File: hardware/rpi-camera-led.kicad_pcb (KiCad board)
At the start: 2 copper layers, 25 x 23.9 mm, 20 parts, among them J1 FFC 15P 1.0mm (to Raspberry P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, J2 FFC 15P 1.0mm (to camera), J3 Qwiic (JST SH 1.0mm), J4 SWD program header 2.54mm, Q1 AO3400A, Q2 Phototransistor, U1 CH32V003A4M6

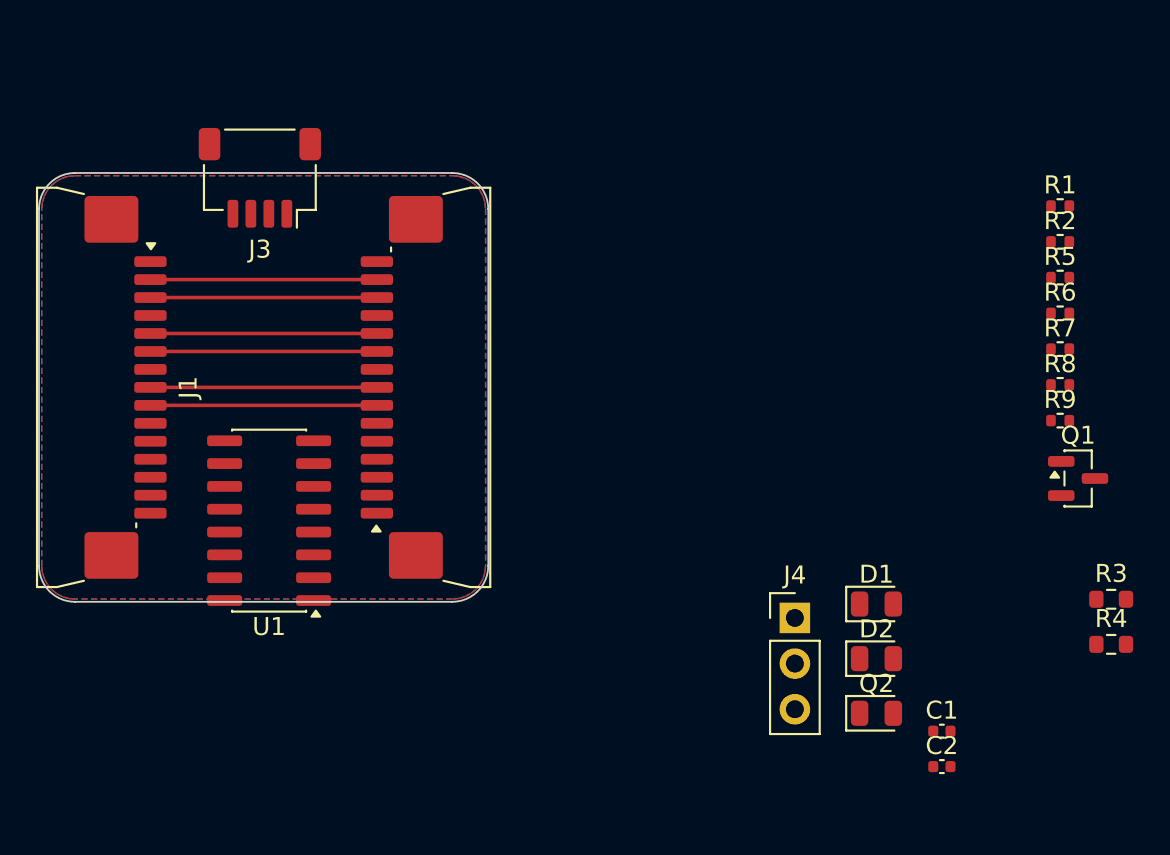
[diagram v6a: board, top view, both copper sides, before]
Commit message: Tim's KiCad session: U1 pins rearranged, bus routing extended
Committing work in progress so it is not lost.  U1's assignment moves
toward the arrangement Tim asked about -- camera GPIOs on pins 7/8, Pi
sense on 9/10, I2C also brought out to 5/6 and 11/12 -- J2 goes back to
the reversed pin mapping, and the board grows to 37 track segments with
unconnected down from 49 to 35.

It does not pass its checks yet.  Recorded here rather than fixed,
because each of these is a design decision:

  * ERC error, U1.13 (PA2) is connected to nothing, with a 0.038mm wire
    fragment left behind at the same point -- the remains of dragging
    CAM_IO1 off that pin.
  * SWIO and CAM_IO1 are the same net.  U1.7 is PD1, the single-wire
    debug pin, and J4.2 sits on it, so KiCad merges the two and keeps
    CAM_IO1.  Programming the part would drive the camera's GPIO1 and
    the camera would fight the debugger.
  * SCL is wired to U1.11 and SDA to U1.12, which are PD7 and PA1.
    Neither can be I2C on this package -- the peripheral only reaches
    PC1/PC2 (pins 1/2), since both AFIO remaps need PD0 or PC5 and the
    SOP-16 bonds out neither.  PD7 is worse than useless here: it is
    NRST until the RST_MODE option byte says otherwise, so a factory
    part would sit in reset for every low half-cycle of SCL.  SDA on
    U1.5 and SCL on U1.6 (PC6/PC7) are inert rather than harmful.
  * Four no-connect flags now dangle where pins used to be.

The board matches the schematic (parity 0), so the same joins exist in
copper: 116 DRC violations.

Co-Authored-By: Claude Opus 5 (1M context) <noreply@anthropic.com>
Claude-Session: https://claude.ai/code/session_01E6VQHygrbAGSqdngQQsBdx
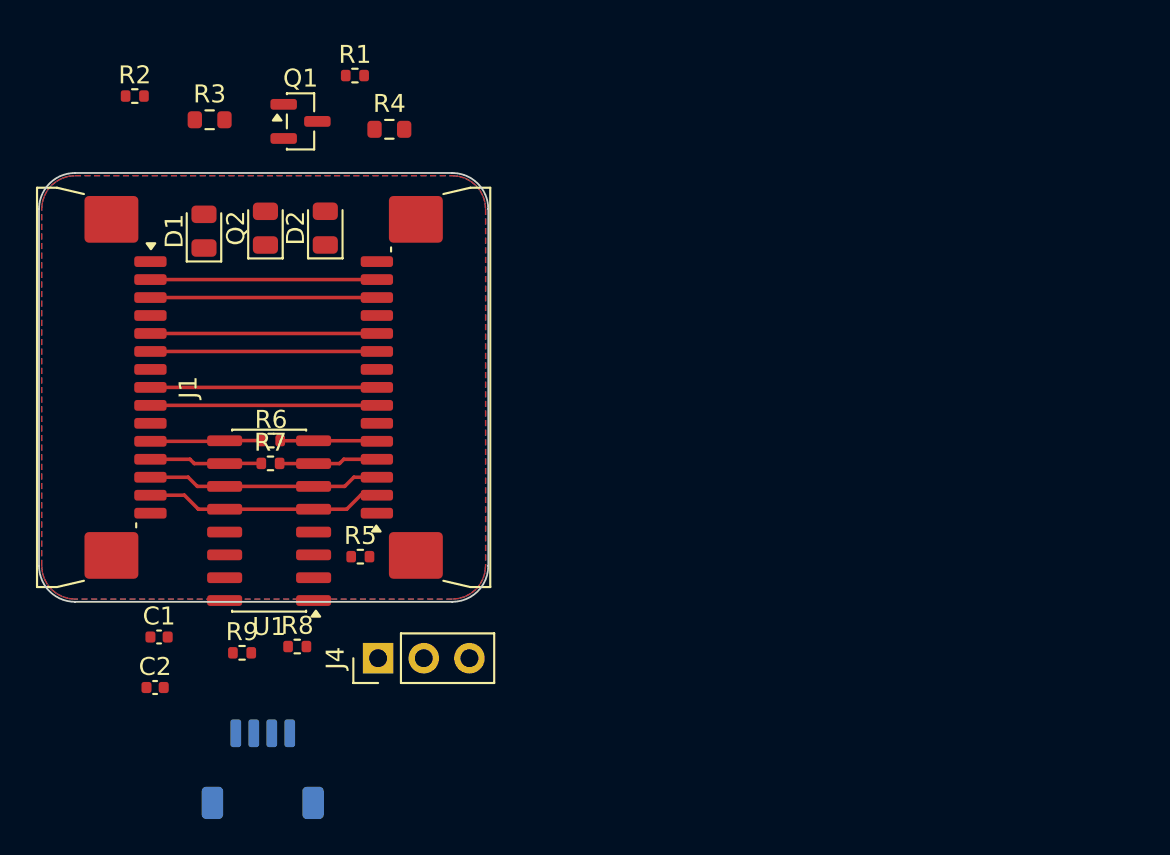
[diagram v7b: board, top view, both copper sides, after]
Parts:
- J3: moved to B.Cu
- moved R3 56.8 mm to (29.5, 17.0)
- moved R2 52.1 mm to (25.3, 15.7)
- moved R4 49.3 mm to (39.5, 17.6)
- moved Q1 47.6 mm to (34.6, 17.1)
- moved R9 47.3 mm to (31.3, 46.7)
- moved R8 44.9 mm to (34.4, 46.4)
- moved R6 44.5 mm to (32.9, 34.9)
- moved R7 44.4 mm to (32.9, 36.2)
- moved C2 44.0 mm to (26.5, 48.6)
- moved C1 43.9 mm to (26.7, 45.8)
- moved Q2 43.4 mm to (32.6, 23.1), turned to 90 degrees
- moved D1 42.8 mm to (29.2, 23.2), turned to 90 degrees
- moved R5 41.9 mm to (37.9, 41.4)
- moved R1 39.9 mm to (37.6, 14.6)
- moved D2 38.9 mm to (35.9, 23.1), turned to 90 degrees
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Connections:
- J2 pad 1: GND -> 3V3
- J2 pad 10: GND -> CAM_D1_P
- J2 pad 11: CAM_IO0 -> CAM_D1_N
- J2 pad 12: CAM_IO1 -> GND
- J2 pad 13: SCL -> CAM_D0_P
- J2 pad 14: SDA -> CAM_D0_N
- J2 pad 15: 3V3 -> GND
- J2 pad 2: CAM_D0_N -> SDA
- J2 pad 3: CAM_D0_P -> SCL
- J2 pad 4: GND -> CAM_IO1
- J2 pad 5: CAM_D1_N -> CAM_IO0
- J2 pad 6: CAM_D1_P -> GND
- J2 pad 7: GND -> CAM_CK_P
- J2 pad 9: CAM_CK_P -> GND
- J4 pad 2: SWIO -> CAM_IO1
- U1 pad 10: PI_IO0 -> PI_IO1
- U1 pad 11: unconnected-(U1-PD7-Pad11) -> SCL
- U1 pad 12: CAM_IO0 -> SDA
- U1 pad 13: CAM_IO1 -> unconnected-(U1-PA2-Pad13)
- U1 pad 5: unconnected-(U1-PC6-Pad5) -> SDA
- U1 pad 6: unconnected-(U1-PC7-Pad6) -> SCL
- U1 pad 7: SWIO -> CAM_IO1
- U1 pad 8: unconnected-(U1-PD4-Pad8) -> CAM_IO0
- U1 pad 9: PI_IO1 -> PI_IO0
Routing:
- net SDA: track 0.00 -> 13.2 mm
- net SCL: track 0.00 -> 13.0 mm
- net PI_IO1: track 0.00 -> 6.27 mm
- net PI_IO0: track 0.00 -> 6.22 mm
- net CAM_IO1: track 0.00 -> 5.51 mm
- net CAM_IO0: track 0.00 -> 5.40 mm

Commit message: J2 becomes the top-contact part, so both cables are standard
With J1 and J2 both bottom-contact, the camera-side cable segment had to
be a same-side (type 1) FFC -- not a part you can buy as a Raspberry Pi
camera cable.  Making J2 top-contact means the interposer flips which
face of the cable carries copper, and both segments become ordinary
opposite-side Raspberry Pi camera cables.

The reasoning, since it is easy to get backwards:

  - the Raspberry Pi's CSI socket is top-contact (SFW15R-2STE1LF) and
    the camera module's is bottom-contact (per Gert van Loo, who
    designed the camera board), which is exactly why the standard cable
    is opposite-side -- "type 2" in JUSHUO's and Gert's numbering;
  - cutting one continuous cable anywhere yields one same-side half and
    one opposite-side half, so an interposer whose two connectors want
    copper on the SAME face forces one odd cable, and one that wants it
    on OPPOSITE faces takes two standard cables;
  - F.Cu + bottom contact wants copper down, F.Cu + top contact wants
    copper up.  J1 bottom / J2 top is therefore the pairing that works.

Nothing moves.  The two variants share a land pattern (verified against
both JUSHUO drawings in fd472db), so this is metadata only: pad 1 is
still at 26.200,24.931 on J1 and 38.800,38.931 on J2, alignment is still
0.000000mm, both pad columns are still 6.3000mm off centre, and DRC
still reports 0 schematic-parity issues.  The existing routing and the
reversed J1.k <-> J2.(16-k) netlist stay valid -- that mapping connects
the pads that physically face each other, which is both the straight
route and the electrically transparent one.

Contact side is now stated everywhere it can be misread: in each
symbol's Value, in the MPN (with LCSC codes and the Amphenol
equivalents, which differ between the two), and as a BOTTOM CONTACT /
TOP CONTACT marker on F.Fab.

check_schematic.py still fails, unchanged and for unrelated reasons:
its EXPECTED table still describes the old pin-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
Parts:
- J1: value FFC 15P 1.0mm (to Raspberry Pi) -> FFC 15P 1.0mm bottom contact (to Raspberry Pi)
- J2: value FFC 15P 1.0mm (to camera) -> FFC 15P 1.0mm top contact (to camera); footprint Connector_FFC-FPC:JUSHUO_AFA07-S15FCA-00_1x15-1MP_P1.0mm_Horizontal -> rpi-camera-led:JUSHUO_AFA07-S15ECA-00_1x15-1MP_P1.0mm_Horizontal
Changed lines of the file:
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@@
 			)
 		)
-		(property "Value" "FFC 15P 1.0mm (to Raspberry Pi)"
+		(property "Value" "FFC 15P 1.0mm bottom contact (to Raspberry Pi)"
 			(at 0 5.68 270)
 			(layer "F.Fab")
@@
 			)
 		)
-		(property "MPN" "JUSHUO AFA07-S15FCA-00 / Amphenol SFW15R-1STE1LF"
+		(property "MPN" "JUSHUO AFA07-S15FCA-00 (LCSC C262721) / Amphenol SFW15R-1STE1LF"
 			(at 0 0 270)
 			(unlocked yes)
@@
 					(size 1 1)
 					(thickness 0.15)
+				)
+			)
+		)
+		(fp_text user "BOTTOM CONTACT"
+			(at 0 1.9 90)
+			(layer "F.Fab")
+			(effects
+				(font
+					(size 0.7 0.7)
+					(thickness 0.1)
 				)
 			)
@@
 		)
 	)
-	(footprint "Connector_FFC-FPC:JUSHUO_AFA07-S15FCA-00_1x15-1MP_P1.0mm_Horizontal"
+	(footprint "rpi-camera-led:JUSHUO_AFA07-S15ECA-00_1x15-1MP_P1.0mm_Horizontal"
 		(layer "F.Cu")
 		(at 42.175 31.931 90)
-		(descr "JUSHUO FPC connector, 15 bottom-side contacts, 1.0mm pitch, 2.5mm height, SMT, https://www.lcsc.com/datasheet/lcsc_datasheet_2304140030_JUSHUO-AFA07-S04FCA-00_C262710.pdf")
-		(tags "jushuo fpc")
+		(descr "JUSHUO AFA07-S15ECA-00, 15-way 1.0mm-pitch FFC/FPC ZIF connector, right angle, UPPER (top) contacts: the mated cable's exposed copper must face UP, away from this board. Same land pattern as the bottom-contact AFA07-S15FCA-00. LCSC C262742. https://www.lcsc.com/datasheet/lcsc_datasheet_2304140030_JUSHUO-AFA07-S15ECA-00_C262742.pdf")
+		(tags "jushuo fpc ffc zif upper contact top contact")
 		(property "Reference" "J2"
 			(at 0 -5.48 90)
@@
 			)
 		)
-		(property "Value" "FFC 15P 1.0mm (to camera)"
+		(property "Value" "FFC 15P 1.0mm top contact (to camera)"
 			(at 0 5.68 90)
 			(layer "F.Fab")
@@
 			)
 		)
-		(property "MPN" "JUSHUO AFA07-S15FCA-00 / Amphenol SFW15R-1STE1LF"
+		(property "MPN" "JUSHUO AFA07-S15ECA-00 (LCSC C262742) / Amphenol SFW15R-2STE1LF"
 			(at 0 0 90)
 			(unlocked yes)
@@
 			(layer "F.Fab")
 		)
+		(fp_text user "TOP CONTACT"
+			(at 0 1.9 90)
+			(layer "F.Fab")
+			(effects
+				(font
+					(size 0.7 0.7)
+					(thickness 0.1)
+				)
+			)
+		)
 		(pad "1" smd roundrect
